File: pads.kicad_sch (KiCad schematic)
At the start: 52 parts, among them J1 5V, J10 5V, J11 5V, J12 5V, J13 5V, J14 5V, J15 5V, J16 5V, J17 5V, J18 5V, J19 5V, J2 5V, J20 5V, J21 5V, J22 5V, J23 5V, J24 5V, J25 5V, J26 5V, J27 5V, J28 5V, J29 5V, J3 5V, J30 5V, J35 5V, J36 5V, J37 5V, J38 5V, J39 5V, J4 5V, J40 5V, J41 5V, J42 5V, J43 5V, J44 5V, J45 5V, J46 5V, J47 5V, J48 5V, J5 5V, J53 5V, J54 5V, J55 5V, J56 5V, J57 5V, J58 5V, J6 5V, J7 5V, J8 5V, J9 5V, P1 SM08B-SRSS-TB(LF)(SN), U1 SM06B-SRSS-TB(LF)(SN)

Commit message: Switched to RP2354A and re-routed
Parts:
- removed J10, J11, J12, J54, J55, J57, J58: 5V, lib:small_pad, symbol Connector_Generic:Conn_01x01
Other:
- note added: "RSSI"
- note removed: "2 open ADCs"
- note removed: "Extra power connections"

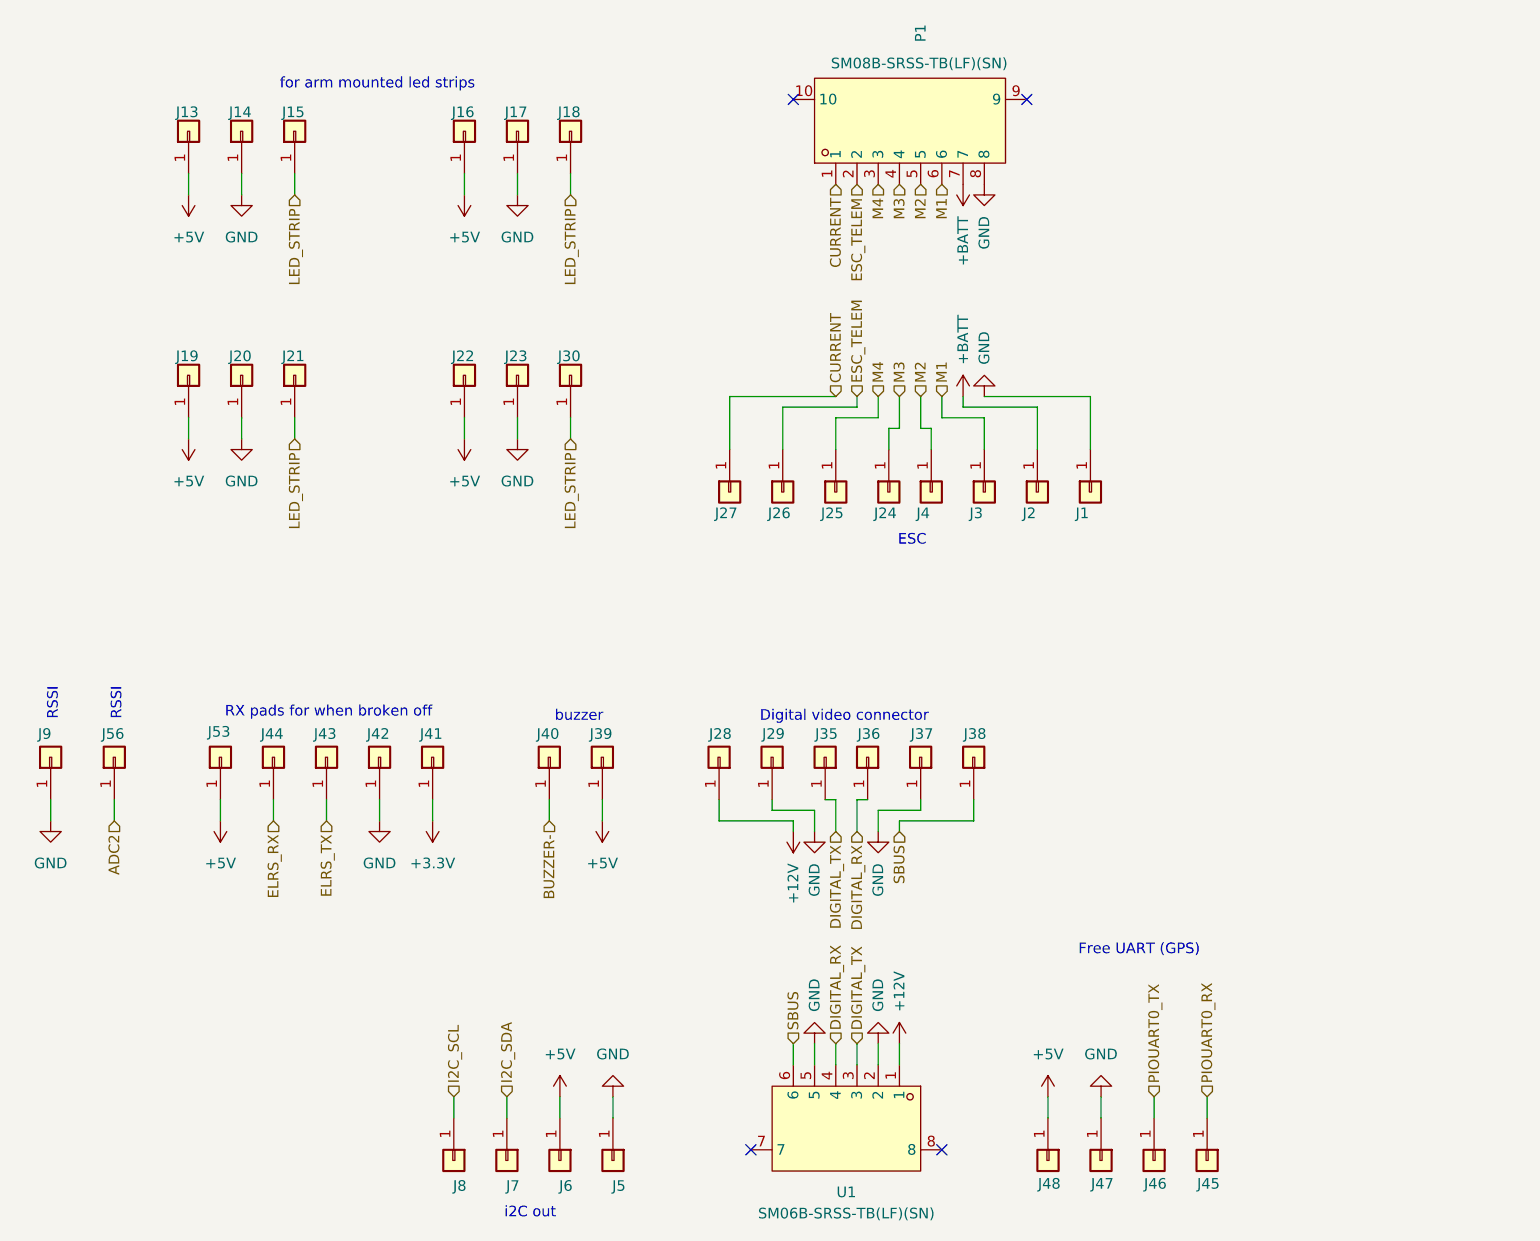
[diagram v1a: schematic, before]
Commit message: Added Open-OSD-X and new layout
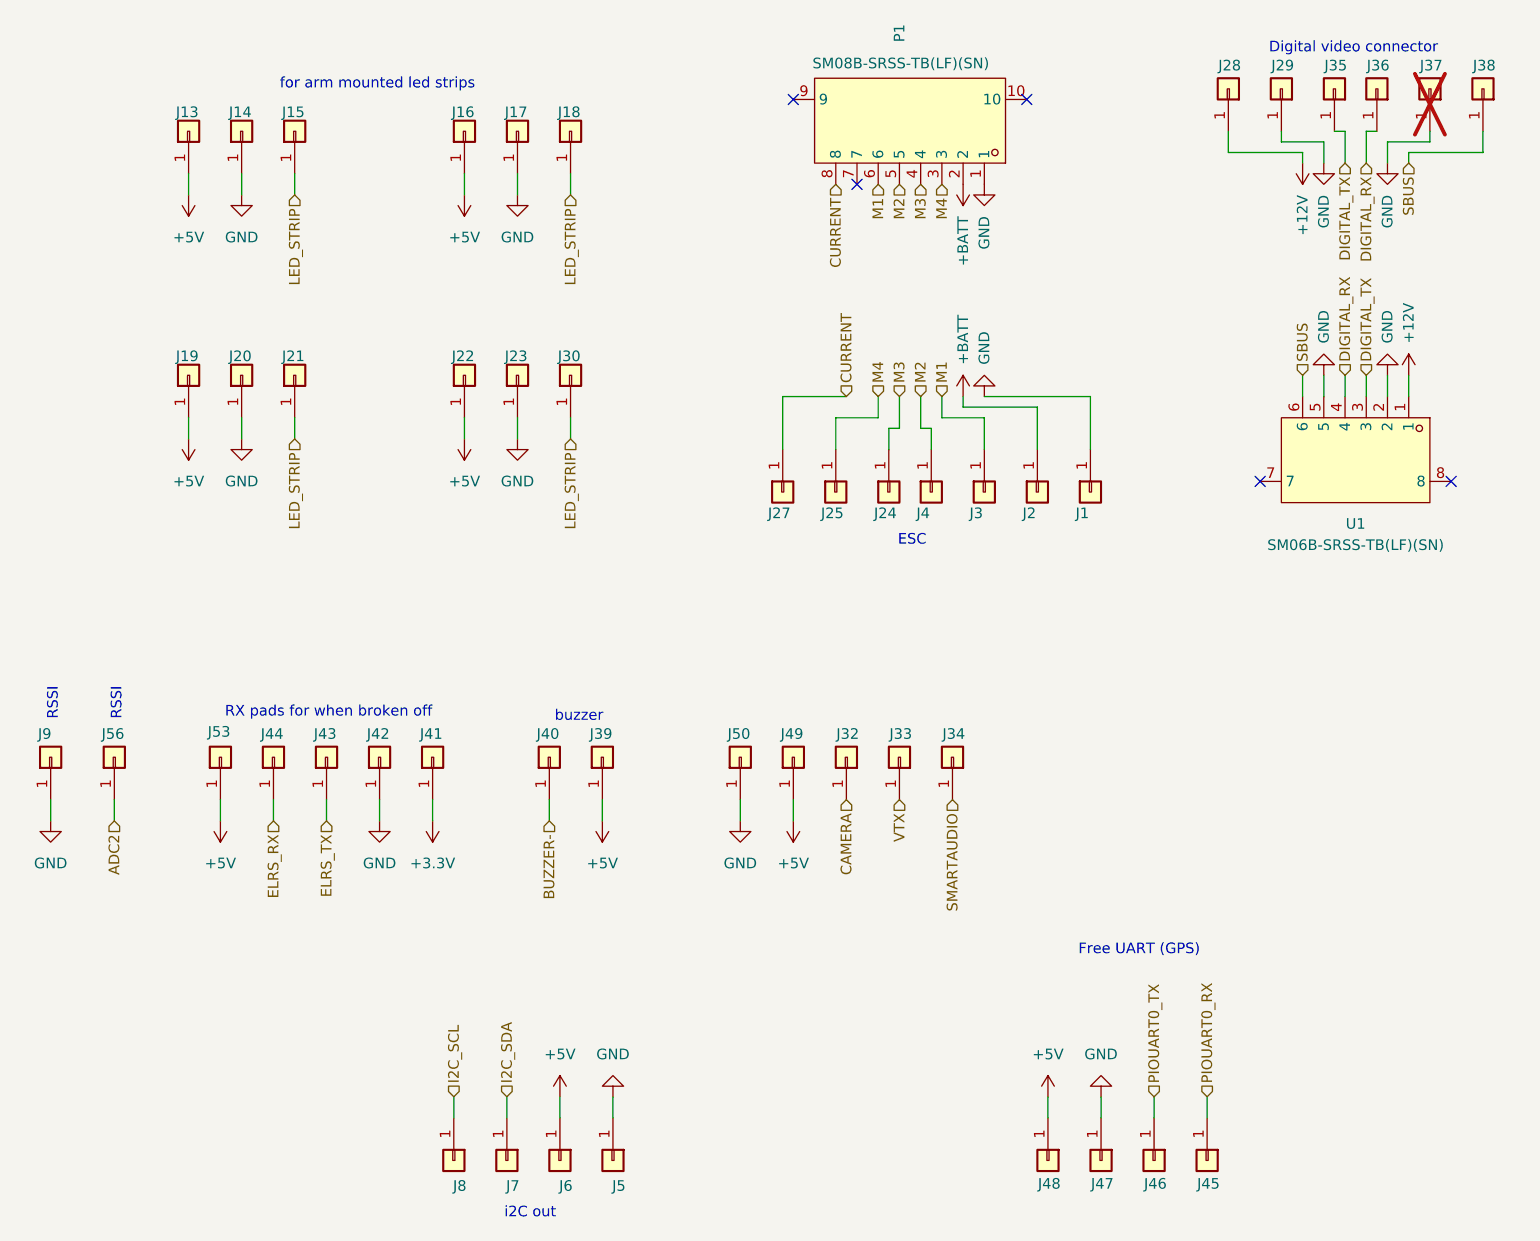
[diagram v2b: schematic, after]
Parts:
- removed J26: 5V, lib:small_pad, symbol Connector_Generic:Conn_01x01
- added J32, J33, J34, J49, J50: 5V, lib:small_pad, symbol Connector_Generic:Conn_01x01
- J37: now not fitted
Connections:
- net ESC_TELEM is gone; now on net +BATT: P1.2
- net +5V: now also J49.1 (Pin_1)
- net +BATT: no longer P1.7
- net CURRENT: now also P1.8; no longer P1.1
- net GND: now also P1.1, J50.1 (Pin_1); no longer P1.8
- new net CAMERA: J32.1 (Pin_1)
- new net SMARTAUDIO: J34.1 (Pin_1)
- new net VTX: J33.1 (Pin_1)
- no-connect marks 4 -> 5
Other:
- moved on the sheet: J27, J28, J29, J35, J36, J38, P1, U1

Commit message: Ordered first revision
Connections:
- net GND: now also P1.10, P1.9, U1.7, U1.8
- no-connect marks 5 -> 1

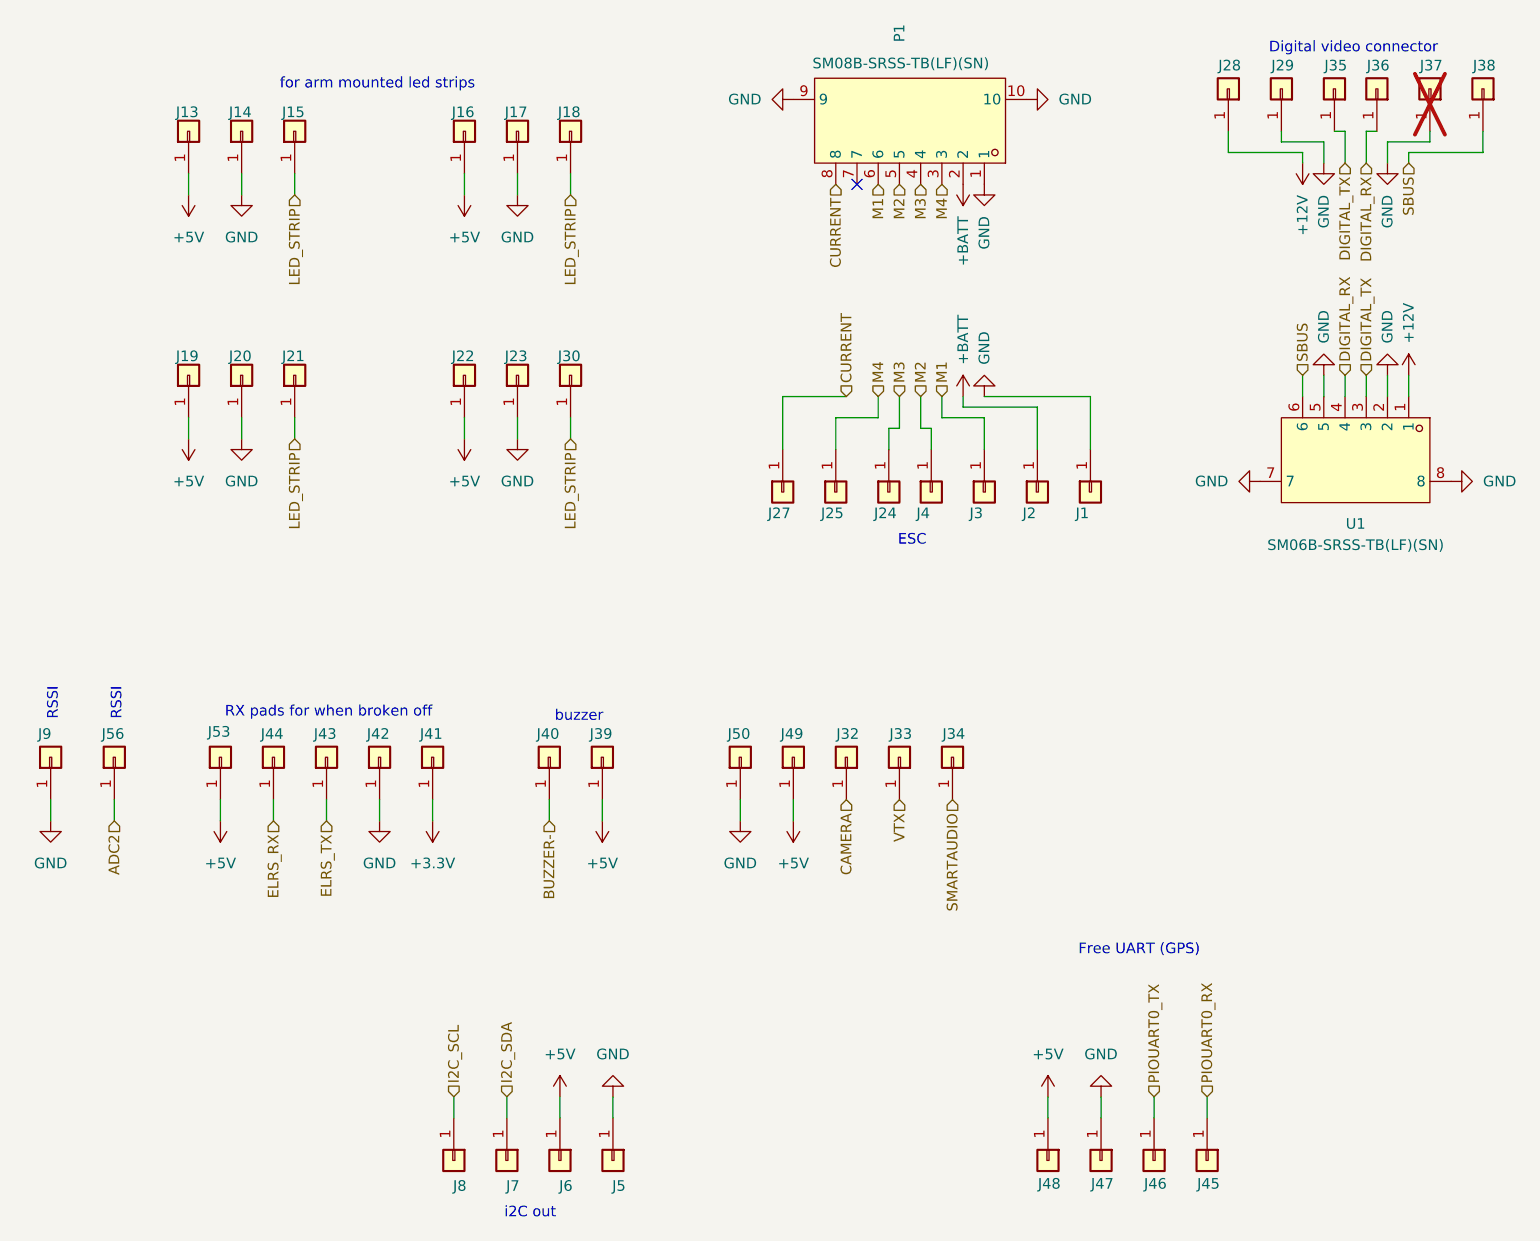
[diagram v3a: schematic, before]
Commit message: Switched to RP2354B for V2 of the FC for more IO. I want to try implement OSD on PIO state machine. I know BF already uses all of them but it should be possible and then later try to combine it witht the WS2812 protocol PIO2. If anybody here has any experience with analog OSD generation let me know, I just want to make a circuit that would allow further software development later. The reason I want to do it this way is it's cheap BOM<1 euro and low footprint, just 2 2x2 IC's and some passives.
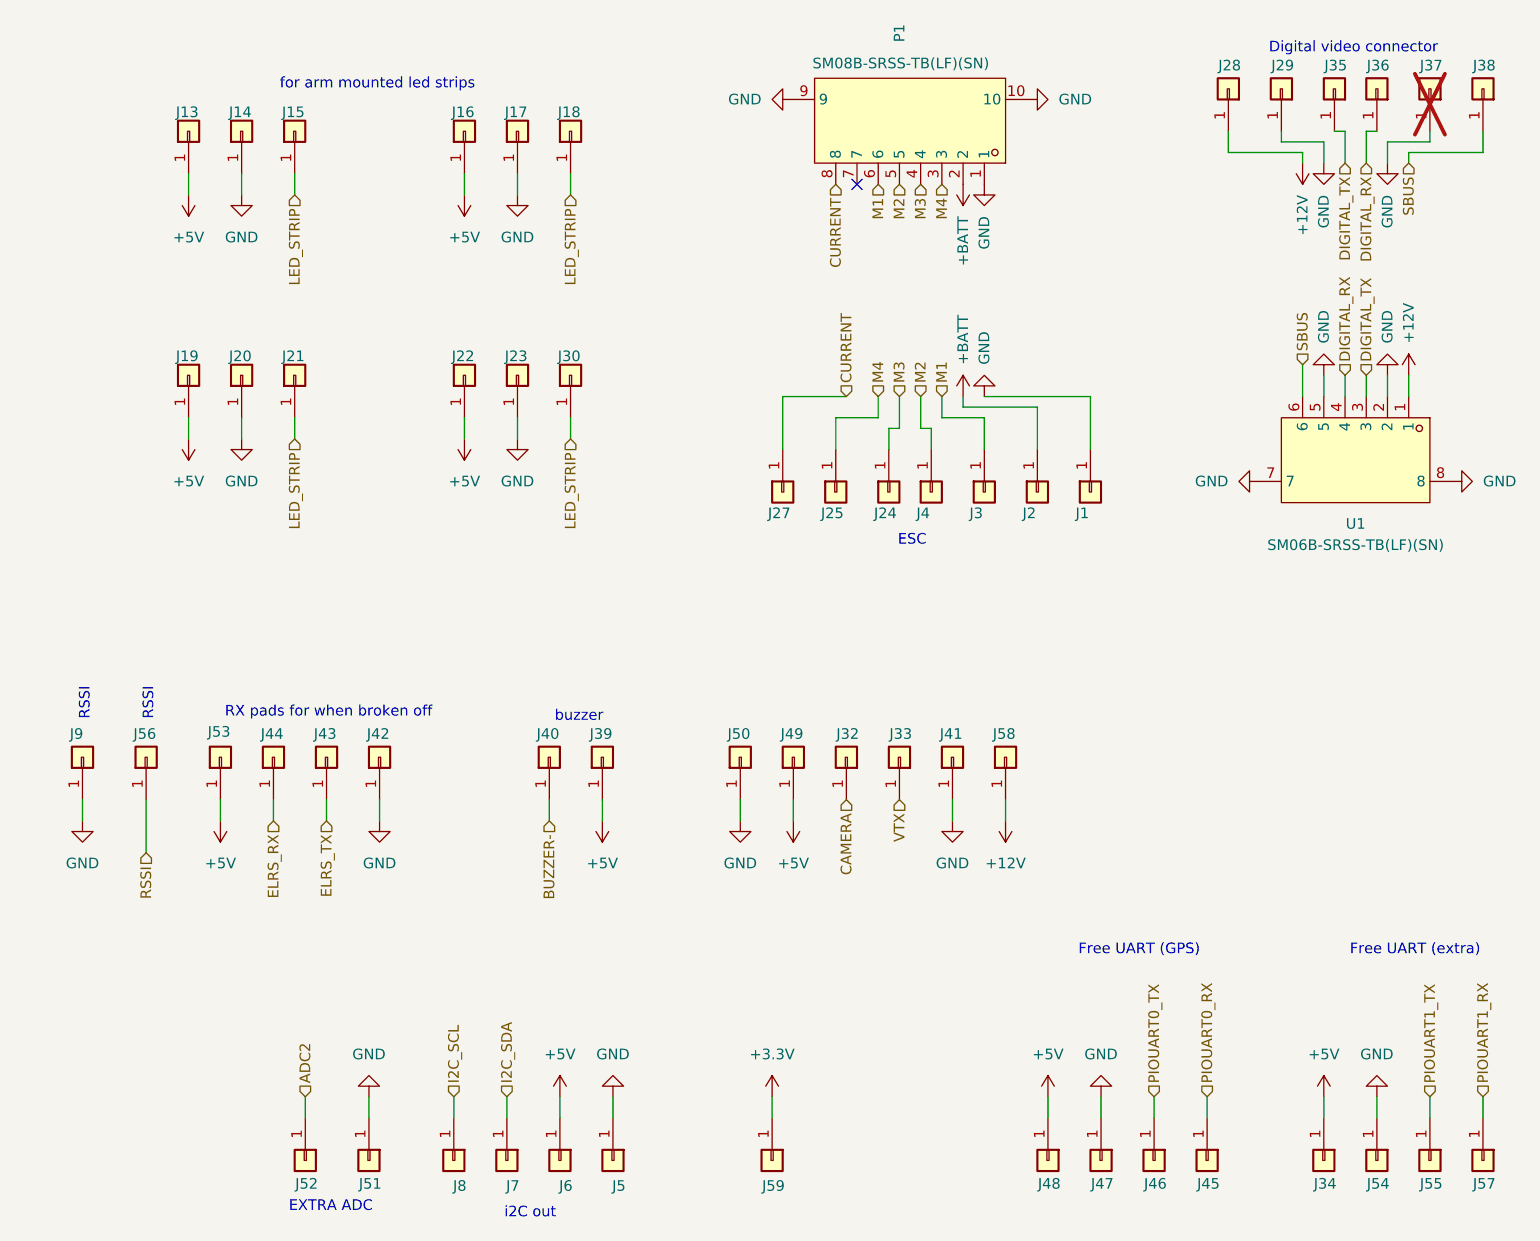
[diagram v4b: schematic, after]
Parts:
- added J51, J52, J54, J55, J57, J58, J59: 5V, lib:small_pad, symbol Connector_Generic:Conn_01x01
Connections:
- net SMARTAUDIO is gone; now on net +5V: J34.1 (Pin_1)
- net +12V: now also J58.1 (Pin_1)
- net +3.3V: now also J59.1 (Pin_1); no longer J41.1 (Pin_1)
- net ADC2: now also J52.1 (Pin_1); no longer J56.1 (Pin_1)
- net GND: now also J41.1 (Pin_1), J51.1 (Pin_1), J54.1 (Pin_1)
- new net PIOUART1_RX: J57.1 (Pin_1)
- new net PIOUART1_TX: J55.1 (Pin_1)
- new net RSSI: J56.1 (Pin_1)
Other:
- note added: "EXTRA ADC"
- note added: "Free UART (extra)"
- moved on the sheet: J56, J9
